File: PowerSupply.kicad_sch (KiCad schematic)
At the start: 16 parts, among them J7 Barrel_Jack_MountingPin, U5 AP63203WU, U6 AP63205WU

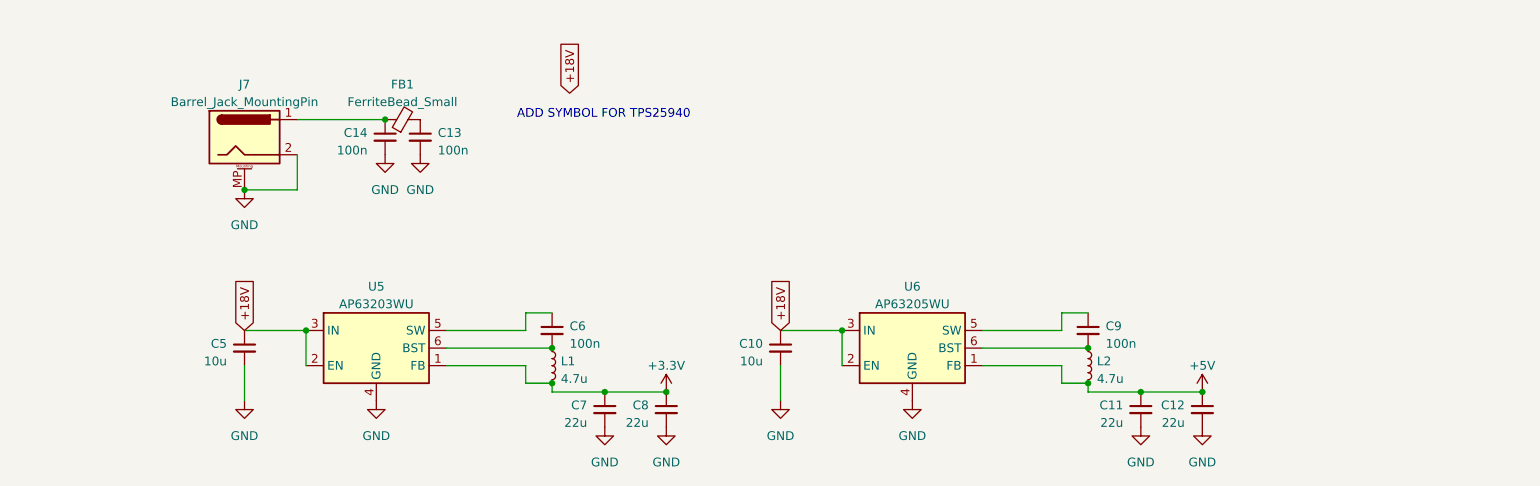
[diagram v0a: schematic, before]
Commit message: Added nrf5340 and pi filters on output of switching supplies
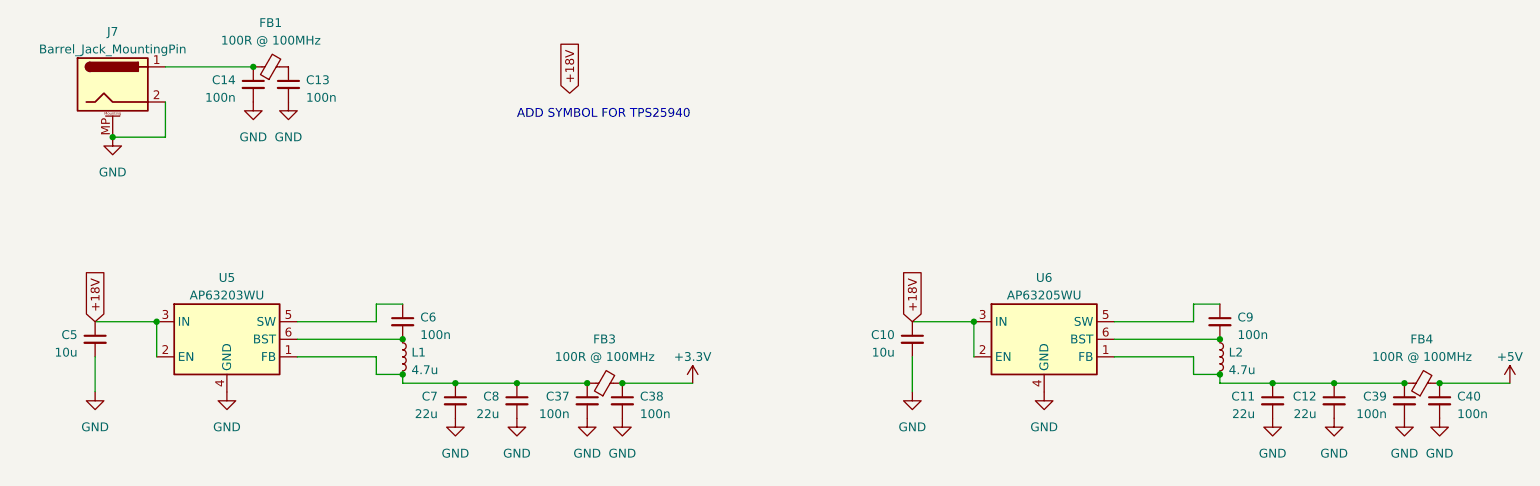
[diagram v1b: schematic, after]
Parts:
- added C37, C38, C39, C40: 100n, symbol Device:C_Small
- added FB3, FB4: 100R @ 100MHz, symbol Device:FerriteBead_Small
- FB1: value FerriteBead_Small -> 100R @ 100MHz
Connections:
- net +3.3V: now also C38.1, FB3.2; no longer C7.1, C8.1, L1.2, U5.1 (FB)
- net +5V: now also C40.1, FB4.2; no longer C11.1, C12.1, L2.2, U6.1 (FB)
- net GND: now also C37.2, C38.2, C39.2, C40.2
- new net: C11.1, C12.1, C39.1, FB4.1, L2.2, U6.1 (FB)
- new net: C37.1, C7.1, C8.1, FB3.1, L1.2, U5.1 (FB)
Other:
- moved on the sheet: C10, C11, C12, C13, C14, C5, C6, C7, C8, C9, FB1, J7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

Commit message: 10/09/23 - Schematic v0.1
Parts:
- added D1: D_TVS, symbol Device:D_TVS
- added F2: 3A, symbol Device:Polyfuse_Small
- J7: footprint (none) -> Connector_BarrelJack:BarrelJack_CUI_PJ-036AH-SMT_Horizontal
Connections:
- net +18V: now also F2.2
- net GND: now also D1.1 (A1)
- net at C14.1, FB1.1, J7.1: now also D1.2 (A2)
- net at C13.1, FB1.2: now also F2.1
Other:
- note removed: "ADD SYMBOL FOR TPS25940"
- moved on the sheet: C13, C14, FB1
